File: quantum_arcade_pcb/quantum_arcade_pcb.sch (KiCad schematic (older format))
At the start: 482 parts, among them J20 J20, Q10 2N3904, Q11 2N3904, Q12 2N3906, Q13 2N3904, Q14 2N3904, Q15 2N6044, Q16 2N6044, Q17 2N3904, Q7 2N3904, Q8 2N3906, Q9 2N3904, SW1 SW_DIP_x08, SW2 SW_DIP_x08, Y1 12.096MHz

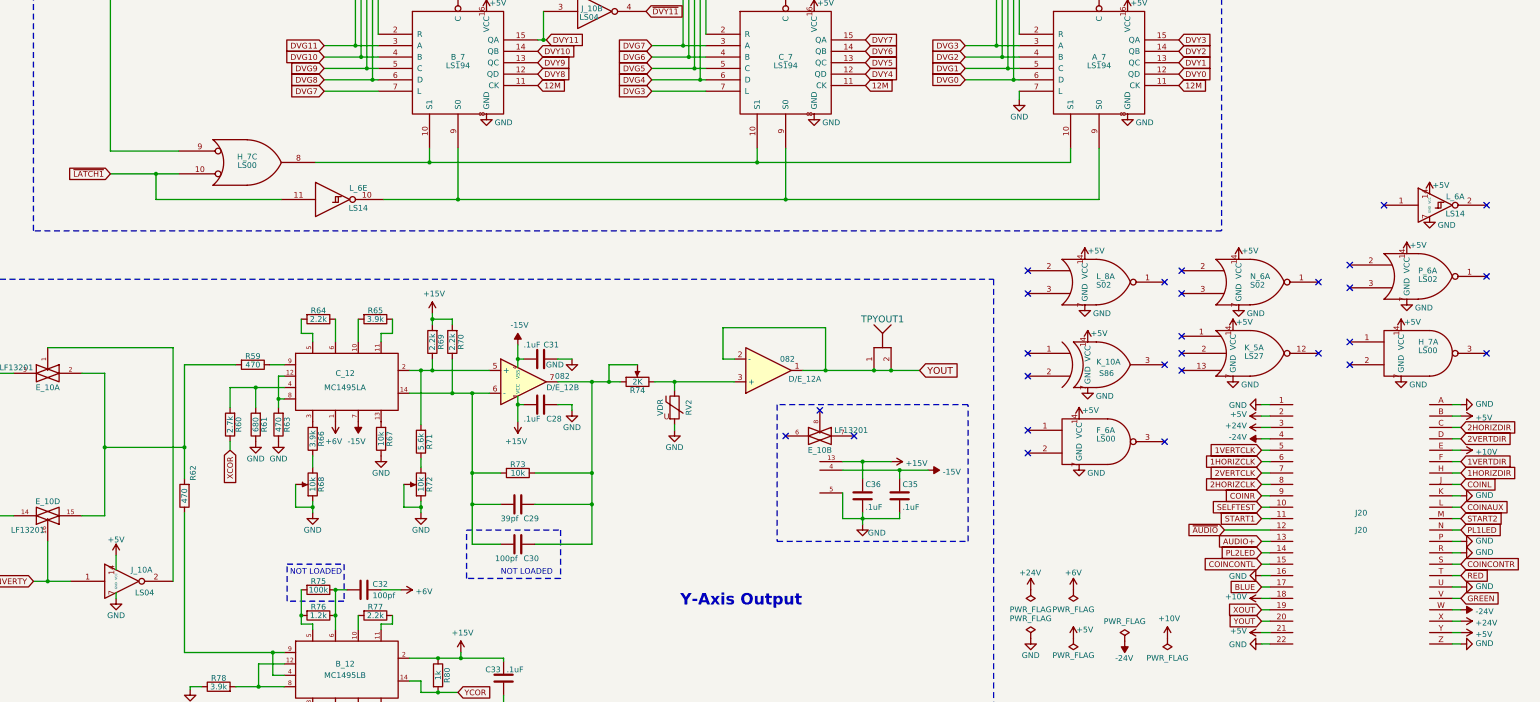
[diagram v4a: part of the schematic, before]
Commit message: Added ground plane, 786 disconnected signals remain
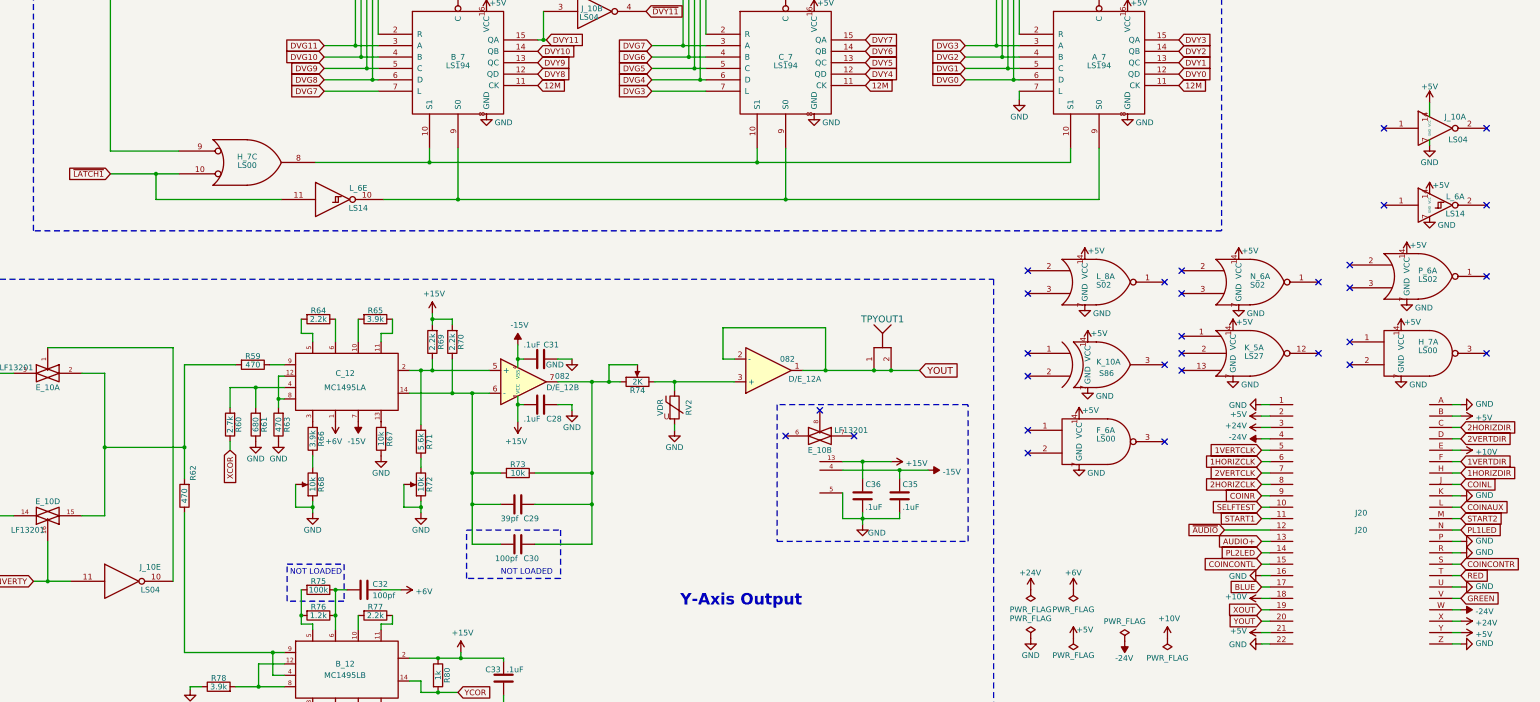
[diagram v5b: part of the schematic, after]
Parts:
- added unit 5 of J_10
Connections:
- net INVERTY: now also J_10.11; no longer J_10.1
- net at E_10.1: now also J_10.10; no longer J_10.2
- no-connect marks 112 -> 114
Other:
- moved on the sheet: J_10A
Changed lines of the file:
@@
 Connection ~ 40500 28675
 Wire Wire Line
-	33700 30425 33700 30300
+	45225 26450 45225 26325
 Wire Wire Line
-	33700 30625 33700 30675
+	45225 26650 45225 26700
 Text GLabel 28950 29775 2    60   Input ~ 0
 YREF
@@
 L power:GND #PWR?
 U 1 1 64DD9EC2
-P 33700 30675
+P 45225 26700
 AR Path="/638E8E88/64DD9EC2" Ref="#PWR?"  Part="1"
 AR Path="/64DD9EC2" Ref="#PWR0250"  Part="1"
-F 0 "#PWR0250" H 33700 30425 50  0001 C CNN
-F 1 "GND" H 33700 30525 50  0000 C CNN
-F 2 "" H 33700 30675 50  0001 C CNN
-F 3 "" H 33700 30675 50  0001 C CNN
-	1    33700 30675
+F 0 "#PWR0250" H 45225 26450 50  0001 C CNN
+F 1 "GND" H 45225 26550 50  0000 C CNN
+F 2 "" H 45225 26700 50  0001 C CNN
+F 3 "" H 45225 26700 50  0001 C CNN
+	1    45225 26700
 	1    0    0    -1
 $EndComp
@@
 L power:+5V #PWR?
 U 1 1 64DD9F22
-P 33700 30300
+P 45225 26325
 AR Path="/638E8E88/64DD9F22" Ref="#PWR?"  Part="1"
 AR Path="/64DD9F22" Ref="#PWR0261"  Part="1"
-F 0 "#PWR0261" H 33700 30150 50  0001 C CNN
-F 1 "+5V" H 33700 30440 50  0000 C CNN
-F 2 "" H 33700 30300 50  0001 C CNN
-F 3 "" H 33700 30300 50  0001 C CNN
-	1    33700 30300
+F 0 "#PWR0261" H 45225 26175 50  0001 C CNN
+F 1 "+5V" H 45225 26465 50  0000 C CNN
+F 2 "" H 45225 26325 50  0001 C CNN
+F 3 "" H 45225 26325 50  0001 C CNN
+	1    45225 26325
 	1    0    0    -1
 $EndComp
@@
 L Star_Wars_Vector_PCB:LS04 K_?
 U 1 1 64DD9F34
-P 33750 30525
+P 45275 26550
 AR Path="/638E8E88/64DD9F34" Ref="K_?"  Part="1"
 AR Path="/64DD9F34" Ref="J_10"  Part="1"
-F 0 "J_10" H 33925 30625 50  0000 C CNN
-F 1 "LS04" H 33950 30425 50  0000 C CNN
-F 2 "Star_Wars_Vector_PCB:DIP14" H 33750 30525 50  0001 C CNN
-F 3 "" H 33750 30525 50  0001 C CNN
-	1    33750 30525
+F 0 "J_10" H 45450 26650 50  0000 C CNN
+F 1 "LS04" H 45475 26450 50  0000 C CNN
+F 2 "Star_Wars_Vector_PCB:DIP14" H 45275 26550 50  0001 C CNN
+F 3 "" H 45275 26550 50  0001 C CNN
+	1    45275 26550
 	1    0    0    -1
 $EndComp
@@
 	1    0    0    -1
 $EndComp
+$Comp
+L Asteroids:LS04 J_10
+U 5 1 6319E44C
+P 33750 30525
+F 0 "J_10" H 34000 30650 50  0000 C CNN
+F 1 "LS04" H 34000 30450 50  0000 C CNN
+F 2 "" H 33750 30525 50  0001 C CNN
+F 3 "" H 33750 30525 50  0001 C CNN
+	5    33750 30525
+	1    0    0    -1
+$EndComp
+NoConn ~ 45725 26550
+NoConn ~ 44825 26550
 $EndSCHEMATC

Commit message: 592 disconnedted signals remain
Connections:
- net CNTR: now also L_7.11; no longer L_7.10
- net DVY11: now also K_8.10
- net VCTR: now also L_7.10; no longer L_7.11
- net Z2: now also H_8.6 (B1)
- net Z3: now also H_8.3 (A1)
- net ~DVY11: no longer K_8.10
- net ~POR: no longer P_4.13
- net POR: now reaches L_6.4, L_6.5, R_4.2 (1CLR), R_5.2 (1CLR)
- net POR: now also P_4.13
- net at H_8.12 (C2): now also F_8.10 (Q2)
- net at H_8.13 (D2): now also F_8.15 (Q3)
- net at F_8.7 (Q1): now also H_8.5 (B2); no longer H_8.3 (A1)
- no-connect marks 114 -> 112
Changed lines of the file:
@@
 $EndComp
 Text GLabel 8750 7500 0    50   Input ~ 0
-~POR
+POR
 Text GLabel 8750 7300 0    50   Input ~ 0
 UPDATE
@@
 Wire Wire Line
 	27125 27000 27025 27000
-NoConn ~ 26525 24350
-NoConn ~ 26525 24150
 $Comp
 L quantum_arcade_pcb:LS175 F_8
@@
 Wire Wire Line
 	25550 23750 26525 23750
-Wire Wire Line
-	25550 23950 25950 23950
-Wire Wire Line
-	25950 23950 25950 23850
-Wire Wire Line
-	25950 23850 26525 23850
-Wire Wire Line
-	25550 24150 26000 24150
-Wire Wire Line
-	26000 24150 26000 23950
-Wire Wire Line
-	26000 23950 26525 23950
-Wire Wire Line
-	26075 24350 26075 24050
-Wire Wire Line
-	26075 24050 26525 24050
-Wire Wire Line
-	25550 24350 26075 24350
 NoConn ~ 25550 23850
 NoConn ~ 25550 24050
@@
 	24650 23225 24650 23300
 Text GLabel 23325 23125 0    50   Input ~ 0
-~DVY11
+DVY11
 Text GLabel 23325 23325 0    50   Input ~ 0
 ~STATCLK
@@
 Text GLabel 33300 4325 0    50   Input ~ 0
 SCALE
-Text GLabel 33300 4775 0    50   Input ~ 0
-CNTR
 Text GLabel 33300 4925 0    50   Input ~ 0
+CNTR
+Text GLabel 33300 4775 0    50   Input ~ 0
 VCTR
 $Comp
@@
 NoConn ~ 45725 26550
 NoConn ~ 44825 26550
+Text GLabel 18300 3750 2    50   Input ~ 0
+POR
+Wire Wire Line
+	18300 3750 18300 4000
+Text GLabel 26525 23850 0    50   Input ~ 0
+Z3
+Wire Wire Line
+	25550 23950 26525 23950
+Text GLabel 26525 24050 0    50   Input ~ 0
+Z2
+Wire Wire Line
+	25550 24350 26525 24350
+Wire Wire Line
+	25550 24150 26525 24150
 $EndSCHEMATC

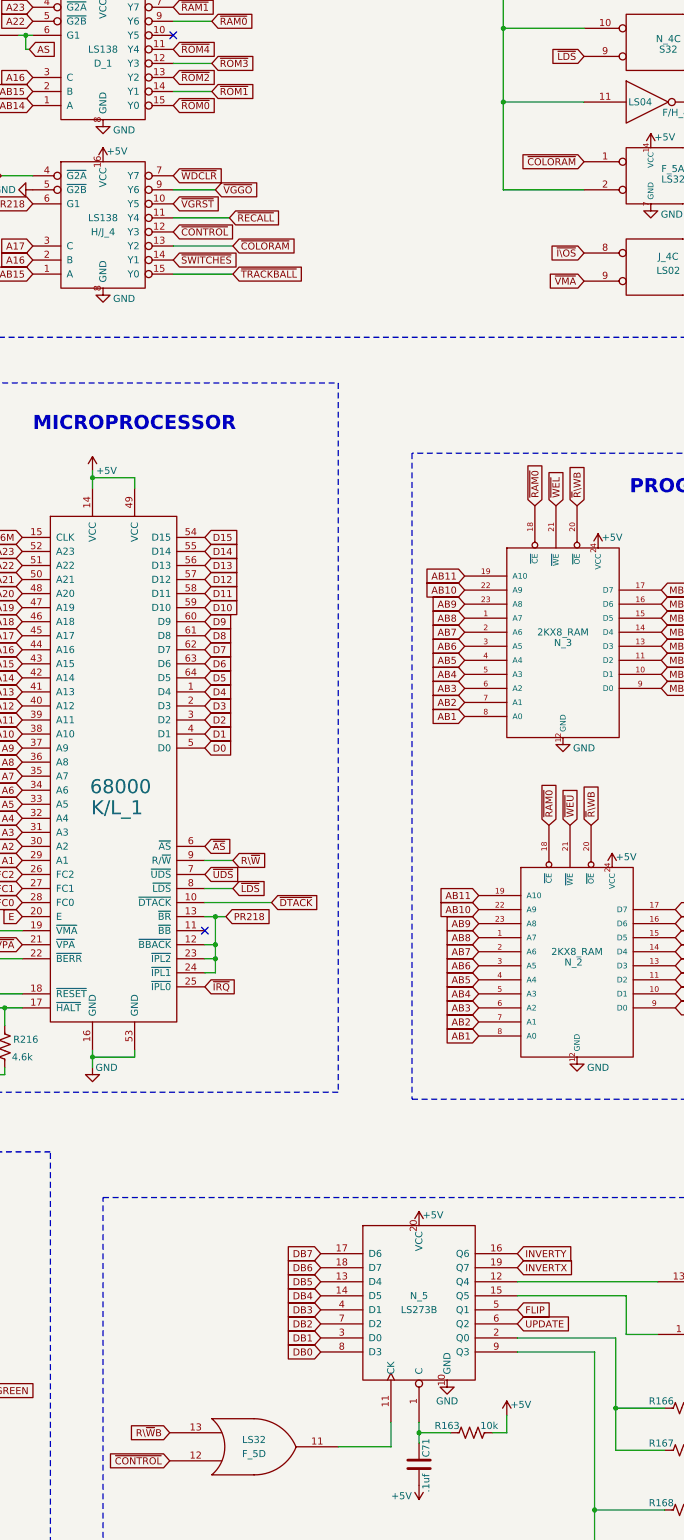
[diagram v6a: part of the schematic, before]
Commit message: 295 disconnedted signals remain
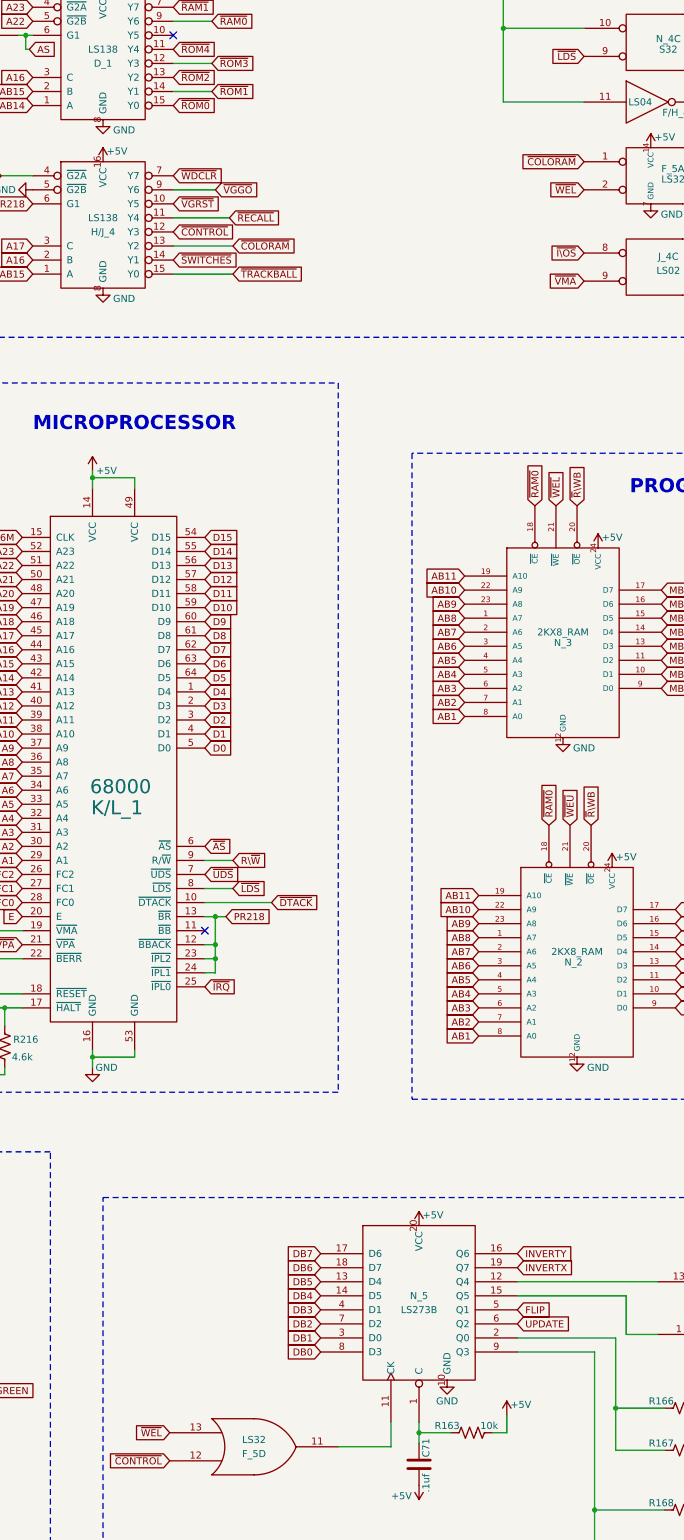
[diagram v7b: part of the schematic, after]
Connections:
- net R\~W~B: no longer F_5.13, F_5.2
- net ~WEL: now also F_5.13, F_5.2
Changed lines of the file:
@@
 	30150 10950 30150 10425
 Connection ~ 30150 10425
-Wire Wire Line
-	30725 11575 30150 11575
-Wire Wire Line
-	30150 11575 30150 10950
-Connection ~ 30150 10950
 Text GLabel 30725 10625 0    50   Input ~ 0
 ~LDS
@@
 Wire Wire Line
 	10700 9575 9825 9575
-Text GLabel 8375 9675 0    50   Input ~ 0
-~WEL
 Wire Wire Line
 	8625 9675 8375 9675
@@
 	29350 20525 28975 20525
 Text GLabel 27775 20425 0    50   Input ~ 0
-R\~W~B
+~WEL
 Text GLabel 27775 20625 0    50   Input ~ 0
 ~CONTROL
@@
 Wire Wire Line
 	25550 24150 26525 24150
+Text GLabel 8375 9675 0    50   Input ~ 0
+~WEL
+Text GLabel 30725 11575 0    50   Input ~ 0
+~WEL
 $EndSCHEMATC

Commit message: 208 disconnedted signals remain
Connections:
- net DVG7: no longer B_7.7 (L)
- net DVY7: now also B_7.7 (L)
- net OP0: no longer J_5.12 (2D)
- net ~OP0: now also J_5.12 (2D)
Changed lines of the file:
@@
 Connection ~ 42325 25225
 Text GLabel 35525 26225 0    50   Input ~ 0
-DVG7
+DVY7
 Wire Wire Line
 	36000 26225 35525 26225
@@
 	34750 4625 34750 4525
 Text GLabel 34225 3875 0    50   Input ~ 0
-OP0
+~OP0
 Text GLabel 34225 4025 0    50   Input ~ 0
 ~STROBE0
